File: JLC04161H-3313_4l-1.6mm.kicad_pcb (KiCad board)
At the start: 4 copper layers, 24 x 24 mm, 3 parts

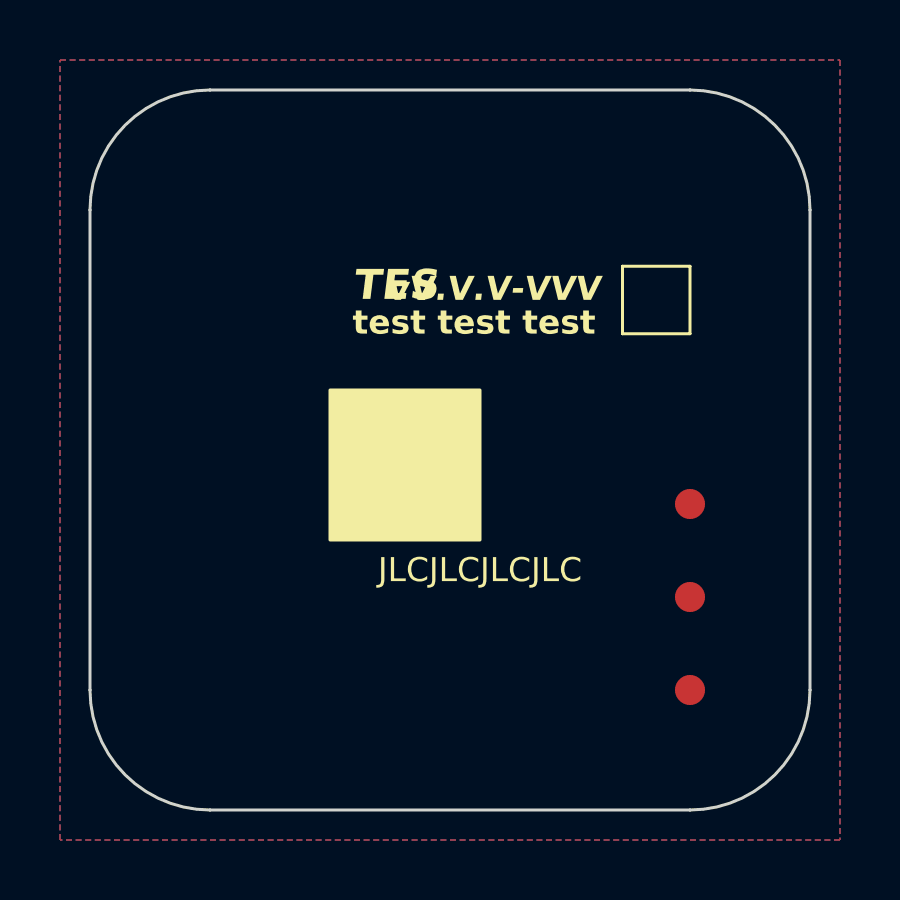
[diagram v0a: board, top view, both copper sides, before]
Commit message: Remove JLCJLCJLCJLC silkscreen text from board layouts
Co-Authored-By: Claude Sonnet 5 <noreply@anthropic.com>
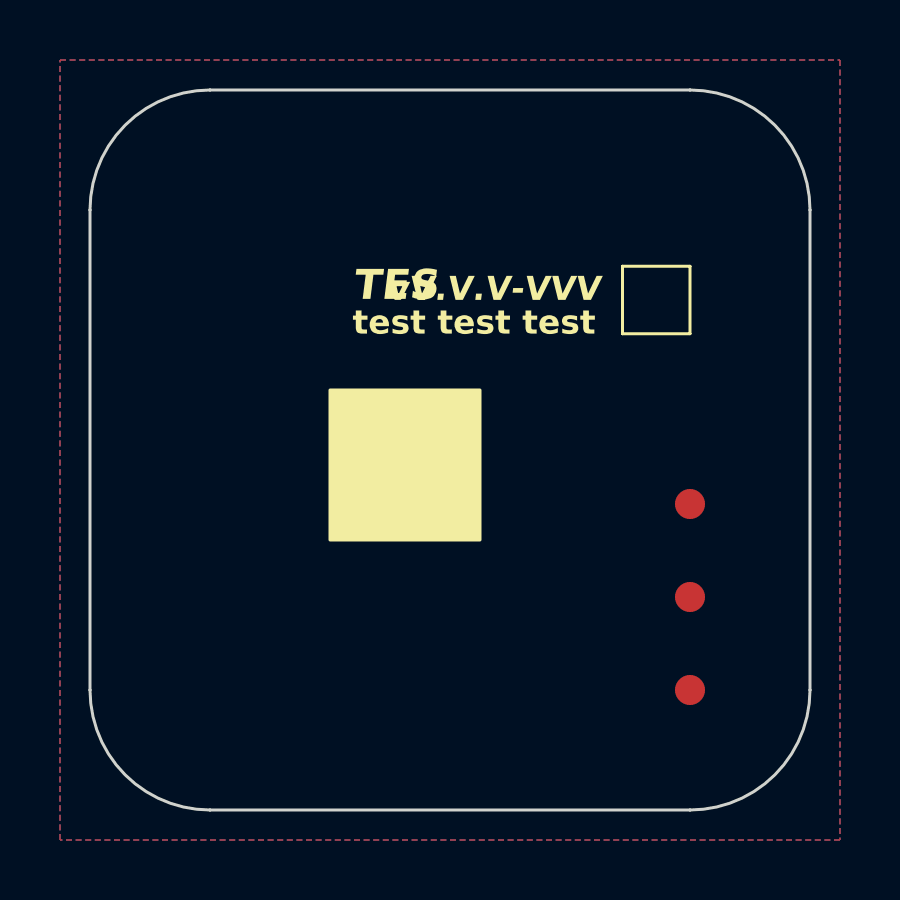
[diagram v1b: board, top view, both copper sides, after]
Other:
- board text removed: "JLCJLCJLCJLC"
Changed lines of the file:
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@@
-		)
-	)
-	(gr_text "JLCJLCJLCJLC"
-		(at 43 46 0)
-		(layer "F.SilkS")
-		(effects
-			(font
-				(size 0.8 0.8)
-				(thickness 0.15)
-			)
 		)
 	)
